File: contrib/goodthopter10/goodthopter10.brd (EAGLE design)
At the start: 54.3 x 21.6 mm, 11 parts, among them IC1 F22X4---DA38, IC2 FT232RL-BASICSSOP, X1 USBPCB

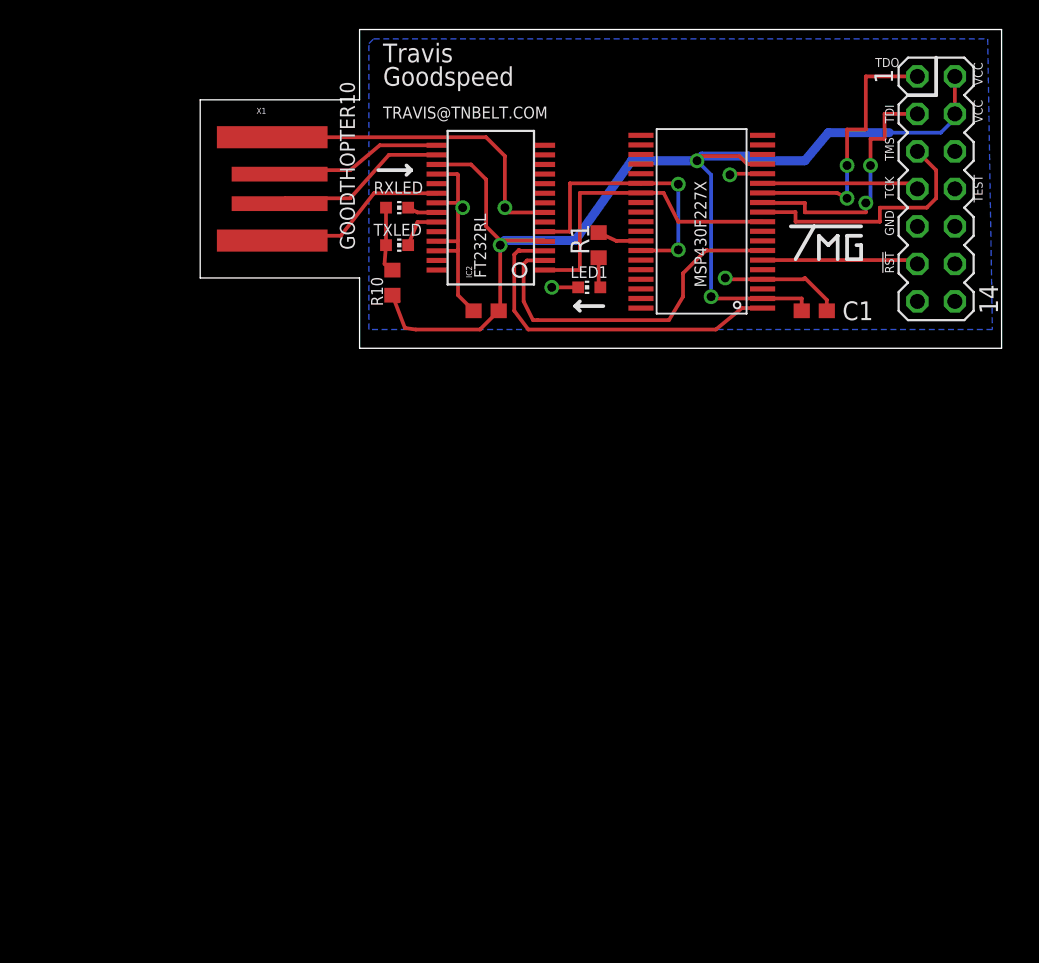
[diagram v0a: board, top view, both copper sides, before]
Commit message: goodthopter10 schematic progress, mcp done and routed
git-svn-id: https://svn.code.sf.net/p/goodfet/code@1194 12e2690d-a6be-4b82-a7b7-67c4a43b65c8
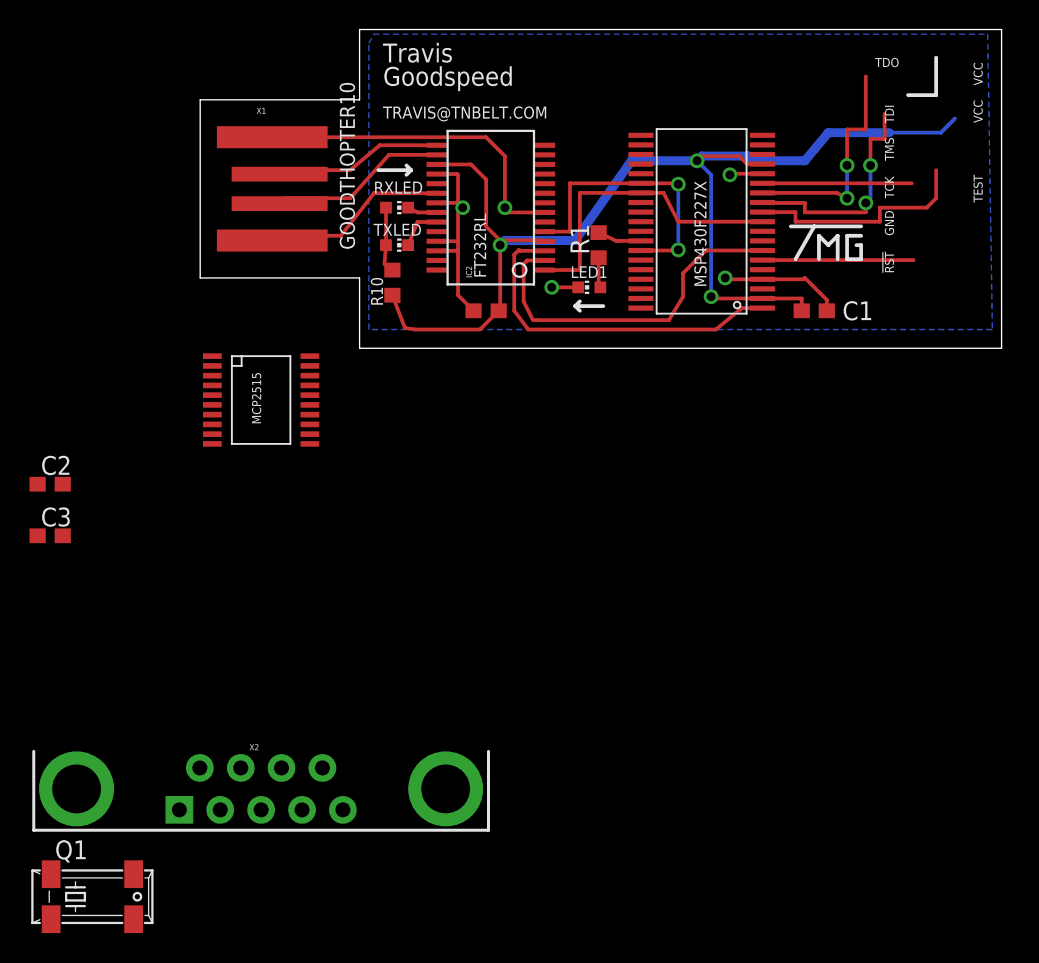
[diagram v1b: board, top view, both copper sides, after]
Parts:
- removed JTAG: (no value), con-lstb:MA07-2
- added C2, C3: (no value), rcl:C0603
- added Q1: (no value), crystal:MM20SS
- added U$1: MCP2515, MCP2515:TSSOP20
- added X2: (no value), SparkFun-Connectors:DB9_MALE
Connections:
- new net OSC1: C3.2, Q1.1, U$1.9
- new net OSC2: C2.2, Q1.4, U$1.8
- new net RXCAN: U$1.2, X2.2
- new net TXCAN: U$1.1, X2.7
- net !CS: now also U$1.18; no longer JTAG.5
- net GND: now also C2.1, C3.1, U$1.10, X2.3; no longer JTAG.9
- net MISO: now also U$1.17; no longer JTAG.1
- net MOSI: now also U$1.16; no longer JTAG.3
- net SCK: now also U$1.14; no longer JTAG.7
- net VCC: now also U$1.20; no longer JTAG.2, JTAG.4
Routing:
- net MISO: track 18.8 -> 15.3 mm
- net VCC: track 85.5 -> 82.7 mm
- net MOSI: track 17.8 -> 15.6 mm
- net !CS: track 17.3 -> 15.5 mm
- net SCK: track 10.6 -> 10.1 mm

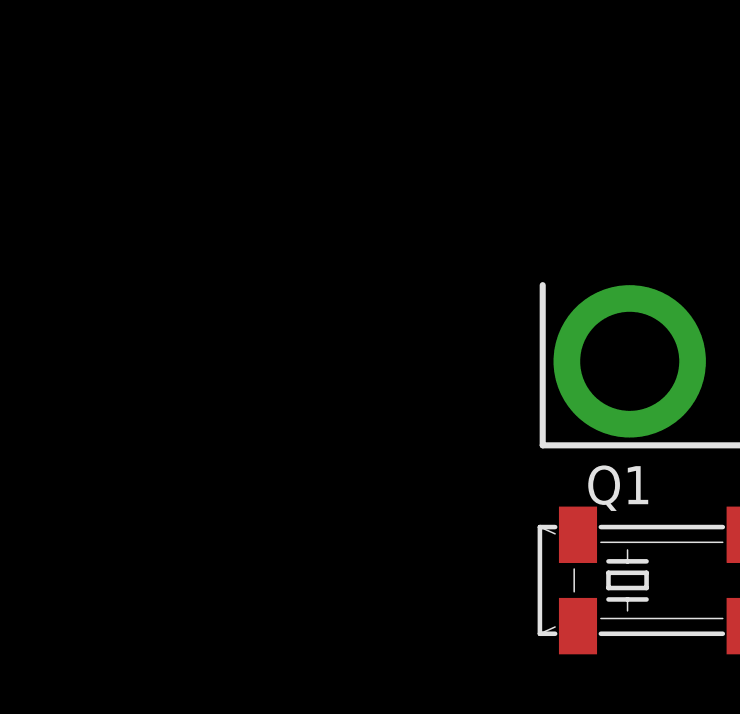
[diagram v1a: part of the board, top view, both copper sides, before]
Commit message: Updated values for crystal circuit (MCP2515).
git-svn-id: https://svn.code.sf.net/p/goodfet/code@1195 12e2690d-a6be-4b82-a7b7-67c4a43b65c8
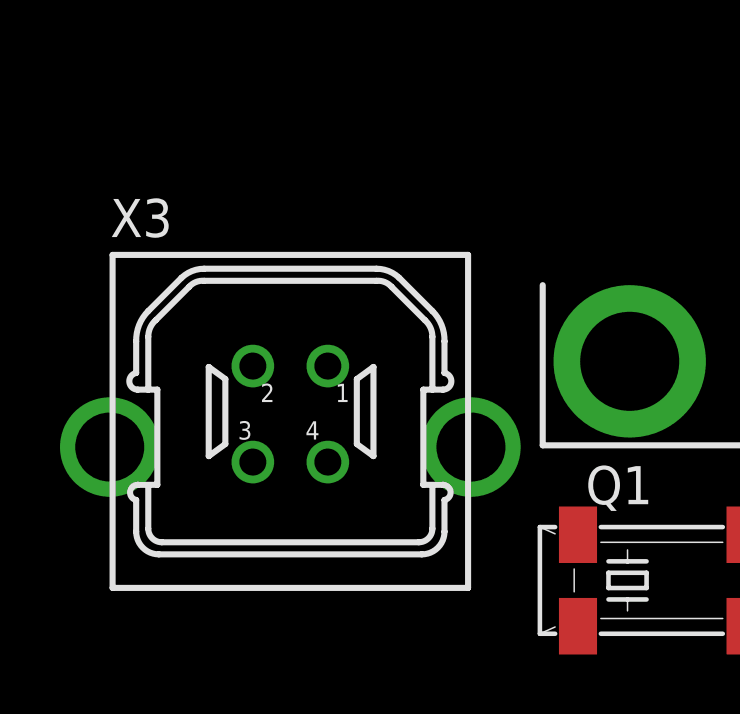
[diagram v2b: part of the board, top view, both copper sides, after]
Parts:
- added X3: KUSBVX-BS1N, con-kycon:KUSBVX-BS1N
- C2, C3: value (none) -> 15pF
- Q1: value (none) -> 20MHz
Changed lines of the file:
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@@
 </element>
 <element name="U$1" library="MCP2515" package="TSSOP20" value="MCP2515" x="4.1275" y="-2.8575"/>
-<element name="C2" library="rcl" package="C0603" value="" x="-10.16" y="-8.89"/>
-<element name="C3" library="rcl" package="C0603" value="" x="-10.16" y="-12.3825"/>
+<element name="C2" library="rcl" package="C0603" value="15pF" x="-10.16" y="-8.89"/>
+<element name="C3" library="rcl" package="C0603" value="15pF" x="-10.16" y="-12.3825"/>
 <element name="X2" library="SparkFun-Connectors" package="DB9_MALE" value="" x="4.1275" y="-29.5275"/>
-<element name="Q1" library="crystal" package="MM20SS" value="" x="-7.3025" y="-36.83">
+<element name="Q1" library="crystal" package="MM20SS" value="20MHz" x="-7.3025" y="-36.83">
 <attribute name="OC_NEWARK" value="unknown" x="-7.3025" y="-36.83" size="1.778" layer="27" display="off"/>
 <attribute name="MPN" value="" x="-7.3025" y="-36.83" size="1.778" layer="27" display="off"/>
@@
 <attribute name="OC_FARNELL" value="unknown" x="-7.3025" y="-36.83" size="1.778" layer="27" display="off"/>
 </element>
+<element name="X3" library="con-kycon" package="KUSBVX-BS1N" value="KUSBVX-BS1N" x="-19.685" y="-32.385"/>
 </elements>
 <signals>

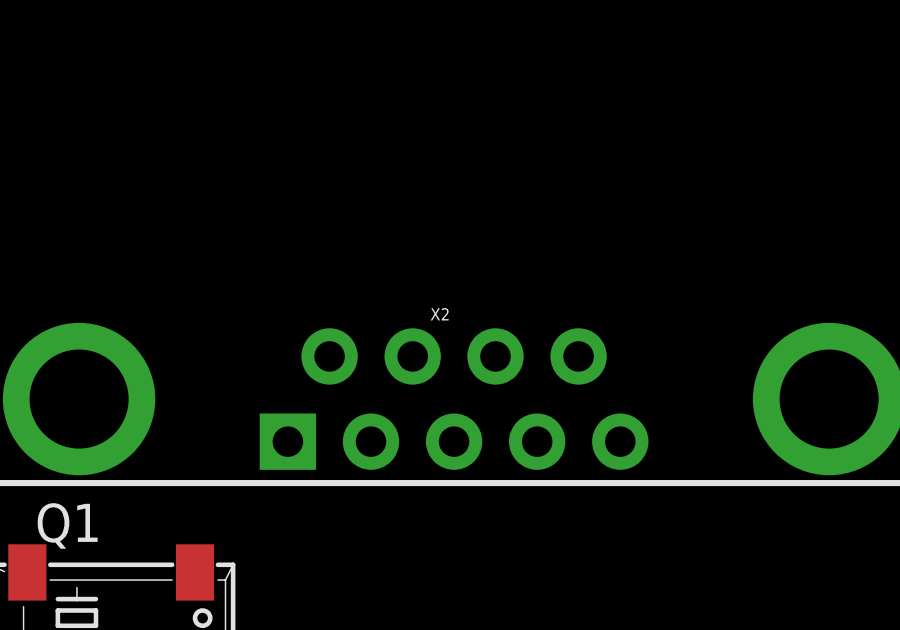
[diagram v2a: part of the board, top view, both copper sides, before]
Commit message: Updated goodthopter schematic, fixing CAN physical connector.
git-svn-id: https://svn.code.sf.net/p/goodfet/code@1196 12e2690d-a6be-4b82-a7b7-67c4a43b65c8
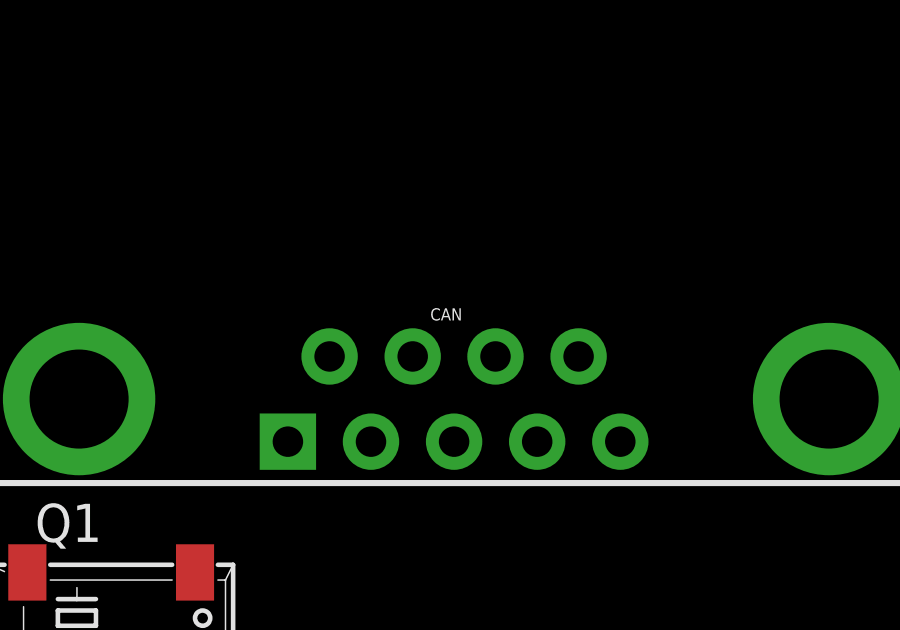
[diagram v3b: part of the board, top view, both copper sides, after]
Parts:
- renumbered X2 to CAN
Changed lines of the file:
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@@
 <element name="C2" library="rcl" package="C0603" value="15pF" x="-10.16" y="-8.89"/>
 <element name="C3" library="rcl" package="C0603" value="15pF" x="-10.16" y="-12.3825"/>
-<element name="X2" library="SparkFun-Connectors" package="DB9_MALE" value="" x="4.1275" y="-29.5275"/>
+<element name="CAN" library="SparkFun-Connectors" package="DB9_MALE" value="" x="4.1275" y="-29.5275"/>
 <element name="Q1" library="crystal" package="MM20SS" value="20MHz" x="-7.3025" y="-36.83">
 <attribute name="OC_NEWARK" value="unknown" x="-7.3025" y="-36.83" size="1.778" layer="27" display="off"/>
@@
 <contactref element="C2" pad="1"/>
 <contactref element="C3" pad="1"/>
-<contactref element="X2" pad="3"/>
+<contactref element="CAN" pad="3"/>
 <contactref element="U$1" pad="10"/>
 <wire x1="35.56" y1="5.08" x2="35.56" y2="12.065" width="0" layer="19" extent="16-16"/>
@@
 <signal name="TXCAN">
 <contactref element="U$1" pad="1"/>
-<contactref element="X2" pad="7"/>
+<contactref element="CAN" pad="7"/>
 <wire x1="0.8255" y1="-0.2159" x2="5.5075" y2="-28.1075" width="0" layer="19" extent="1-1"/>
 </signal>
 <signal name="RXCAN">
 <contactref element="U$1" pad="2"/>
-<contactref element="X2" pad="2"/>
+<contactref element="CAN" pad="2"/>
 <wire x1="0.8255" y1="-0.8763" x2="6.8975" y2="-30.9475" width="0" layer="19" extent="1-1"/>
 </signal>

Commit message: Created MCP2551 and USB-TYPE-B Library Parts for GoodThopter10.
git-svn-id: https://svn.code.sf.net/p/goodfet/code@1197 12e2690d-a6be-4b82-a7b7-67c4a43b65c8
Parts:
- removed X1: USBPCB, SparkFun:USB-A-PCB
- removed X3: KUSBVX-BS1N, con-kycon:KUSBVX-BS1N
- added 292304-2: MINI-USB_4P-292304-2, USB-TYPE-B:85-32004-10X
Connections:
- removed net RST: IC1.6
- new net !INT: IC1.27, U$1.13
- new net CAN_SHLD: CAN.5
- new net CAN_V+_OPT: CAN.9
- new net GND_OPT: CAN.6
- new net RSRVD0: CAN.1
- new net RSRVD1: CAN.4
- new net RSRVD2: CAN.8
- net GND: now also 292304-2.4; no longer X1.GND
- net N$3: now also 292304-2.3; no longer X1.USB_P
- net N$4: now also 292304-2.2; no longer X1.USB_M
- net VCC: now also U$1.19
- net VCC5V: now also 292304-2.1; no longer X1.5V
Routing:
- net GND: track 52.6 -> 38.1 mm
- net RST: track 10.2 -> 0.00 mm
- net N$4: track 12.1 -> 11.6 mm
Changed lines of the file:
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@@
 </autorouter>
 <elements>
-<element name="X1" library="SparkFun" package="USB-A-PCB" value="USBPCB" x="5.08" y="11.1125"/>
 <element name="IC2" library="SparkFun" package="SSOP28DB" value="FT232RL-BASICSSOP" x="19.685" y="9.8425" smashed="yes" rot="R90">
 <attribute name="NAME" x="18.415" y="5.08" size="0.4064" layer="25" rot="R90"/>
@@
 <attribute name="OC_FARNELL" value="unknown" x="-7.3025" y="-36.83" size="1.778" layer="27" display="off"/>
 </element>
-<element name="X3" library="con-kycon" package="KUSBVX-BS1N" value="KUSBVX-BS1N" x="-19.685" y="-32.385"/>
+<element name="292304-2" library="USB-TYPE-B" package="85-32004-10X" value="MINI-USB_4P-292304-2" x="-17.145" y="-65.0875">
+<attribute name="OC_NEWARK" value="unknown" x="-17.145" y="-65.0875" size="1.778" layer="27" display="off"/>
+<attribute name="MPN" value="" x="-17.145" y="-65.0875" size="1.778" layer="27" display="off"/>
+<attribute name="MF" value="" x="-17.145" y="-65.0875" size="1.778" layer="27" display="off"/>
+<attribute name="OC_FARNELL" value="unknown" x="-17.145" y="-65.0875" size="1.778" layer="27" display="off"/>
+</element>
 </elements>
 <signals>
@@
 <via x="34.6075" y="3.81" extent="1-16" drill="0.6" shape="square"/>
 <contactref element="U$1" pad="20"/>
+<contactref element="U$1" pad="19"/>
 <wire x1="7.4295" y1="-0.2159" x2="13.8675" y2="1.69" width="0" layer="19" extent="1-1"/>
+<wire x1="7.4295" y1="-0.8763" x2="7.4295" y2="-0.2159" width="0" layer="19" extent="1-1"/>
 </signal>
 <signal name="RXD">
@@
 </signal>
 <signal name="GND">
-<contactref element="X1" pad="GND"/>
 <contactref element="IC2" pad="26"/>
 <contactref element="IC2" pad="25"/>
@@
 <wire x1="20.6375" y1="9.8425" x2="20.6375" y2="9.5175" width="0.254" layer="1"/>
 <wire x1="20.6375" y1="9.8425" x2="20.32" y2="9.8425" width="0.254" layer="16"/>
-<wire x1="4.88" y1="14.6125" x2="19.36" y2="14.6125" width="0.254" layer="1"/>
 <wire x1="19.36" y1="14.6125" x2="20.6375" y2="13.335" width="0.254" layer="1"/>
 <wire x1="20.6375" y1="13.335" x2="20.6375" y2="9.8425" width="0.254" layer="1"/>
@@
 <contactref element="CAN" pad="3"/>
 <contactref element="U$1" pad="10"/>
-<wire x1="35.56" y1="5.08" x2="35.56" y2="12.065" width="0" layer="19" extent="16-16"/>
-<wire x1="25.6025" y1="4.445" x2="35.2425" y2="5.08" width="0" layer="19" extent="1-16"/>
-<wire x1="23.341" y1="9.5175" x2="23.8125" y2="4.445" width="0" layer="19" extent="1-1"/>
-<wire x1="18.0975" y1="9.8425" x2="20.32" y2="9.8425" width="0" layer="19" extent="16-16"/>
-<wire x1="0.8255" y1="-6.1595" x2="17.4625" y2="3.9125" width="0" layer="19" extent="1-1"/>
-<wire x1="-11.01" y1="-8.89" x2="0.8255" y2="-6.1595" width="0" layer="19" extent="1-1"/>
-<wire x1="-11.01" y1="-12.3825" x2="-11.01" y2="-8.89" width="0" layer="19" extent="1-1"/>
-<wire x1="4.1275" y1="-30.9475" x2="-11.01" y2="-12.3825" width="0" layer="19" extent="1-1"/>
+<contactref element="292304-2" pad="4"/>
+<wire x1="4.1275" y1="-30.9475" x2="-14.435" y2="-66.3375" width="0" layer="19" extent="1-1"/>
+<wire x1="-11.01" y1="-12.3825" x2="4.1275" y2="-30.9475" width="0" layer="19" extent="1-1"/>
+<wire x1="-11.01" y1="-8.89" x2="-11.01" y2="-12.3825" width="0" layer="19" extent="1-1"/>
+<wire x1="0.8255" y1="-6.1595" x2="-11.01" y2="-8.89" width="0" layer="19" extent="1-1"/>
+<wire x1="17.4625" y1="3.9125" x2="0.8255" y2="-6.1595" width="0" layer="19" extent="1-1"/>
+<wire x1="20.32" y1="9.8425" x2="18.0975" y2="9.8425" width="0" layer="19" extent="16-16"/>
+<wire x1="23.8125" y1="4.445" x2="23.341" y2="9.5175" width="0" layer="19" extent="1-1"/>
+<wire x1="35.2425" y1="5.08" x2="25.6025" y2="4.445" width="0" layer="19" extent="1-16"/>
+<wire x1="35.56" y1="12.065" x2="35.56" y2="5.08" width="0" layer="19" extent="16-16"/>
 </signal>
 <signal name="N$3">
-<contactref element="X1" pad="USB_P"/>
 <contactref element="IC2" pad="15"/>
 <wire x1="12.1625" y1="14.0675" x2="16.029" y2="14.0675" width="0.254" layer="1"/>
 <wire x1="10.16" y1="12.3825" x2="12.1625" y2="14.0675" width="0.254" layer="1"/>
 <wire x1="5.65" y1="12.3825" x2="10.16" y2="12.3825" width="0.254" layer="1"/>
-<wire x1="5.38" y1="12.1125" x2="5.65" y2="12.3825" width="0.254" layer="1"/>
+<contactref element="292304-2" pad="3"/>
+<wire x1="5.65" y1="12.3825" x2="-14.435" y2="-63.8375" width="0" layer="19" extent="1-1"/>
 </signal>
 <signal name="N$4">
 <contactref element="IC2" pad="16"/>
-<contactref element="X1" pad="USB_M"/>
 <wire x1="12.7825" y1="13.4175" x2="16.029" y2="13.4175" width="0.254" layer="1"/>
 <wire x1="10.16" y1="10.4775" x2="12.7825" y2="13.4175" width="0.254" layer="1"/>
 <wire x1="5.745" y1="10.4775" x2="10.16" y2="10.4775" width="0.254" layer="1"/>
-<wire x1="5.38" y1="10.1125" x2="5.745" y2="10.4775" width="0.254" layer="1"/>
+<contactref element="292304-2" pad="2"/>
+<wire x1="5.745" y1="10.4775" x2="-12.435" y2="-63.8375" width="0" layer="19" extent="1-1"/>
 </signal>
 <signal name="N$6">
@@
 <wire x1="12.585" y1="7.3025" x2="12.485" y2="6.0325" width="0.254" layer="1"/>
 <wire x1="12.485" y1="6.0325" x2="13.0175" y2="5.6125" width="0.254" layer="1"/>
-</signal>
-<signal name="RST">
-<contactref element="IC1" pad="6"/>
-<wire x1="38.0925" y1="6.29" x2="48.32" y2="6.29" width="0.254" layer="1"/>
 </signal>
 <signal name="RTS">
@@
 </signal>
 <signal name="VCC5V">
-<contactref element="X1" pad="5V"/>
 <contactref element="IC2" pad="20"/>
 <wire x1="11.77" y1="10.8175" x2="16.029" y2="10.8175" width="0.254" layer="1"/>
 <wire x1="9.525" y1="7.9375" x2="11.77" y2="10.8175" width="0.254" layer="1"/>
 <wire x1="5.205" y1="7.9375" x2="9.525" y2="7.9375" width="0.254" layer="1"/>
-<wire x1="4.88" y1="7.6125" x2="5.205" y2="7.9375" width="0.254" layer="1"/>
+<contactref element="292304-2" pad="1"/>
+<wire x1="5.205" y1="7.9375" x2="-12.435" y2="-66.3375" width="0" layer="19" extent="1-1"/>
 </signal>
 <signal name="OSC1">
@@
 <wire x1="0.8255" y1="-0.8763" x2="6.8975" y2="-30.9475" width="0" layer="19" extent="1-1"/>
 </signal>
+<signal name="!INT">
+<contactref element="U$1" pad="13"/>
+<contactref element="IC1" pad="27"/>
+<wire x1="7.4295" y1="-4.8387" x2="29.8525" y2="10.19" width="0" layer="19" extent="1-1"/>
+</signal>
+<signal name="GND_OPT">
+<contactref element="CAN" pad="6"/>
+</signal>
+<signal name="RSRVD2">
+<contactref element="CAN" pad="8"/>
+</signal>
+<signal name="CAN_V+_OPT">
+<contactref element="CAN" pad="9"/>
+</signal>
+<signal name="CAN_SHLD">
+<contactref element="CAN" pad="5"/>
+</signal>
+<signal name="RSRVD1">
+<contactref element="CAN" pad="4"/>
+</signal>
+<signal name="RSRVD0">
+<contactref element="CAN" pad="1"/>
+</signal>
 </signals>
